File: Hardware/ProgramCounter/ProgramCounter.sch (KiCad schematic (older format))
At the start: 27 parts, among them J1 Conn_02x08, J2 Conn_02x08, J3 Conn_02x08, J4 Conn_02x08

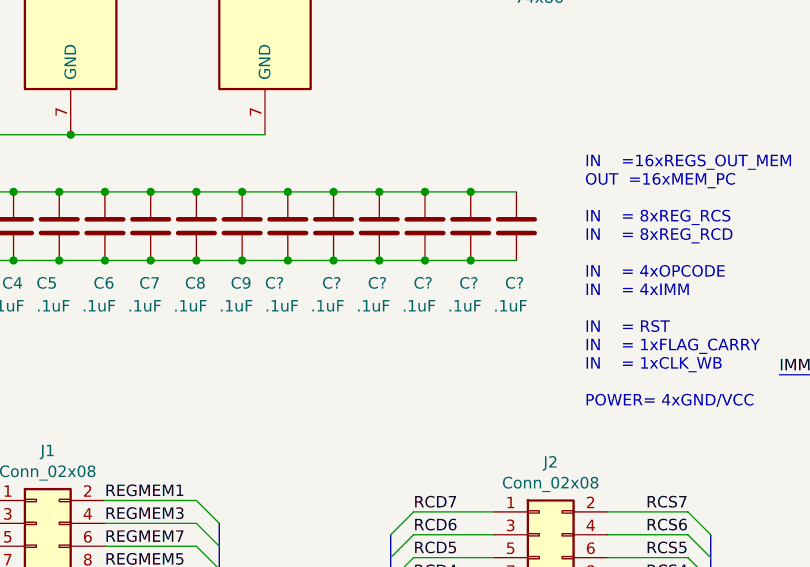
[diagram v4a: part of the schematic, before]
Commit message: PC Board
Mostly done. Going to move register to the right and connect logic gates
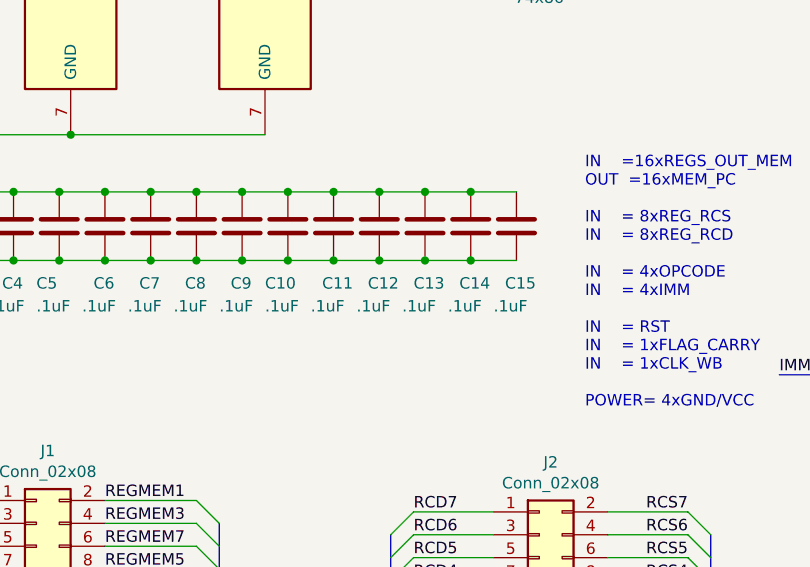
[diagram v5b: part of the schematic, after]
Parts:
- gave numbers to parts that had none: 6
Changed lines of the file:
@@
 $EndComp
 $Comp
-L Device:C C?
+L Device:C C10
 U 1 1 6294B873
 P 2600 5350
-F 0 "C?" H 2500 5100 50  0000 L CNN
+F 0 "C10" H 2500 5100 50  0000 L CNN
 F 1 ".1uF" H 2500 5000 50  0000 L CNN
 F 2 "Capacitor_SMD:C_1206_3216Metric_Pad1.42x1.75mm_HandSolder" H 2638 5200 50  0001 C CNN
@@
 $EndComp
 $Comp
-L Device:C C?
+L Device:C C11
 U 1 1 6294B879
 P 2800 5350
-F 0 "C?" H 2750 5100 50  0000 L CNN
+F 0 "C11" H 2750 5100 50  0000 L CNN
 F 1 ".1uF" H 2700 5000 50  0000 L CNN
 F 2 "Capacitor_SMD:C_1206_3216Metric_Pad1.42x1.75mm_HandSolder" H 2838 5200 50  0001 C CNN
@@
 $EndComp
 $Comp
-L Device:C C?
+L Device:C C12
 U 1 1 6294B87F
 P 3000 5350
-F 0 "C?" H 2950 5100 50  0000 L CNN
+F 0 "C12" H 2950 5100 50  0000 L CNN
 F 1 ".1uF" H 2900 5000 50  0000 L CNN
 F 2 "Capacitor_SMD:C_1206_3216Metric_Pad1.42x1.75mm_HandSolder" H 3038 5200 50  0001 C CNN
@@
 $EndComp
 $Comp
-L Device:C C?
+L Device:C C13
 U 1 1 6294B885
 P 3200 5350
-F 0 "C?" H 3150 5100 50  0000 L CNN
+F 0 "C13" H 3150 5100 50  0000 L CNN
 F 1 ".1uF" H 3100 5000 50  0000 L CNN
 F 2 "Capacitor_SMD:C_1206_3216Metric_Pad1.42x1.75mm_HandSolder" H 3238 5200 50  0001 C CNN
@@
 $EndComp
 $Comp
-L Device:C C?
+L Device:C C14
 U 1 1 6294B88B
 P 3400 5350
-F 0 "C?" H 3350 5100 50  0000 L CNN
+F 0 "C14" H 3350 5100 50  0000 L CNN
 F 1 ".1uF" H 3300 5000 50  0000 L CNN
 F 2 "Capacitor_SMD:C_1206_3216Metric_Pad1.42x1.75mm_HandSolder" H 3438 5200 50  0001 C CNN
@@
 $EndComp
 $Comp
-L Device:C C?
+L Device:C C15
 U 1 1 629609E2
 P 3600 5350
-F 0 "C?" H 3550 5100 50  0000 L CNN
+F 0 "C15" H 3550 5100 50  0000 L CNN
 F 1 ".1uF" H 3500 5000 50  0000 L CNN
 F 2 "Capacitor_SMD:C_1206_3216Metric_Pad1.42x1.75mm_HandSolder" H 3638 5200 50  0001 C CNN

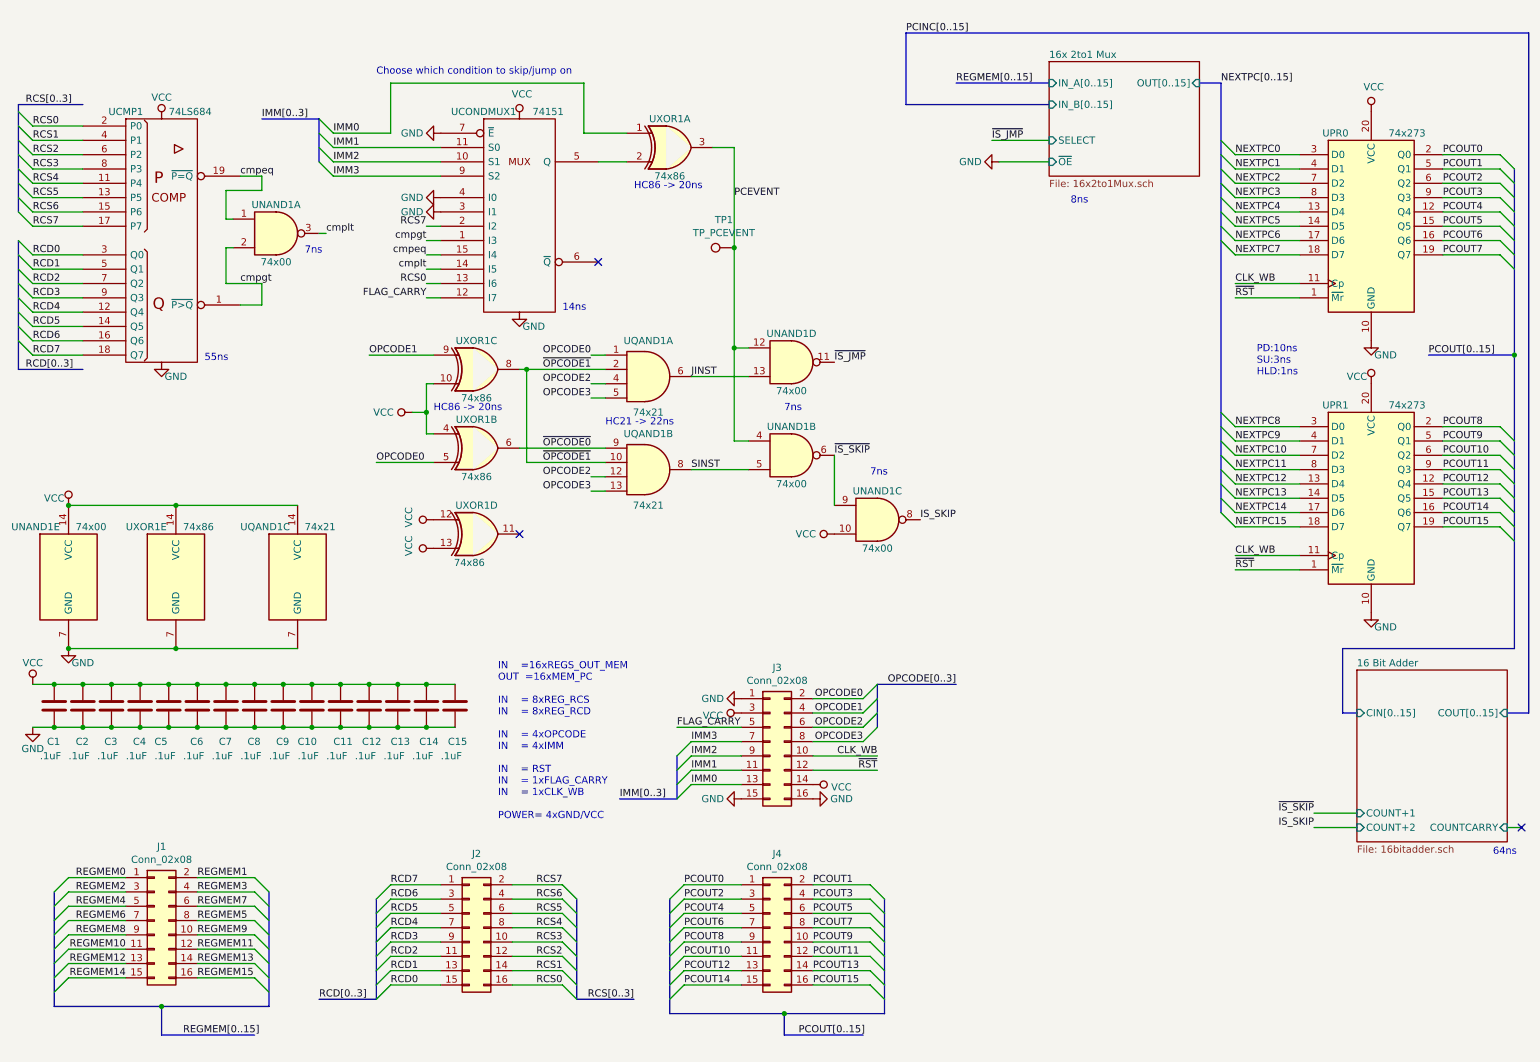
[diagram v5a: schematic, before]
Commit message: Program Counter Board
Seems to be done. Likely be ordering very soon. Also added a debug/testpoint connector to the top so that I can probe it easier
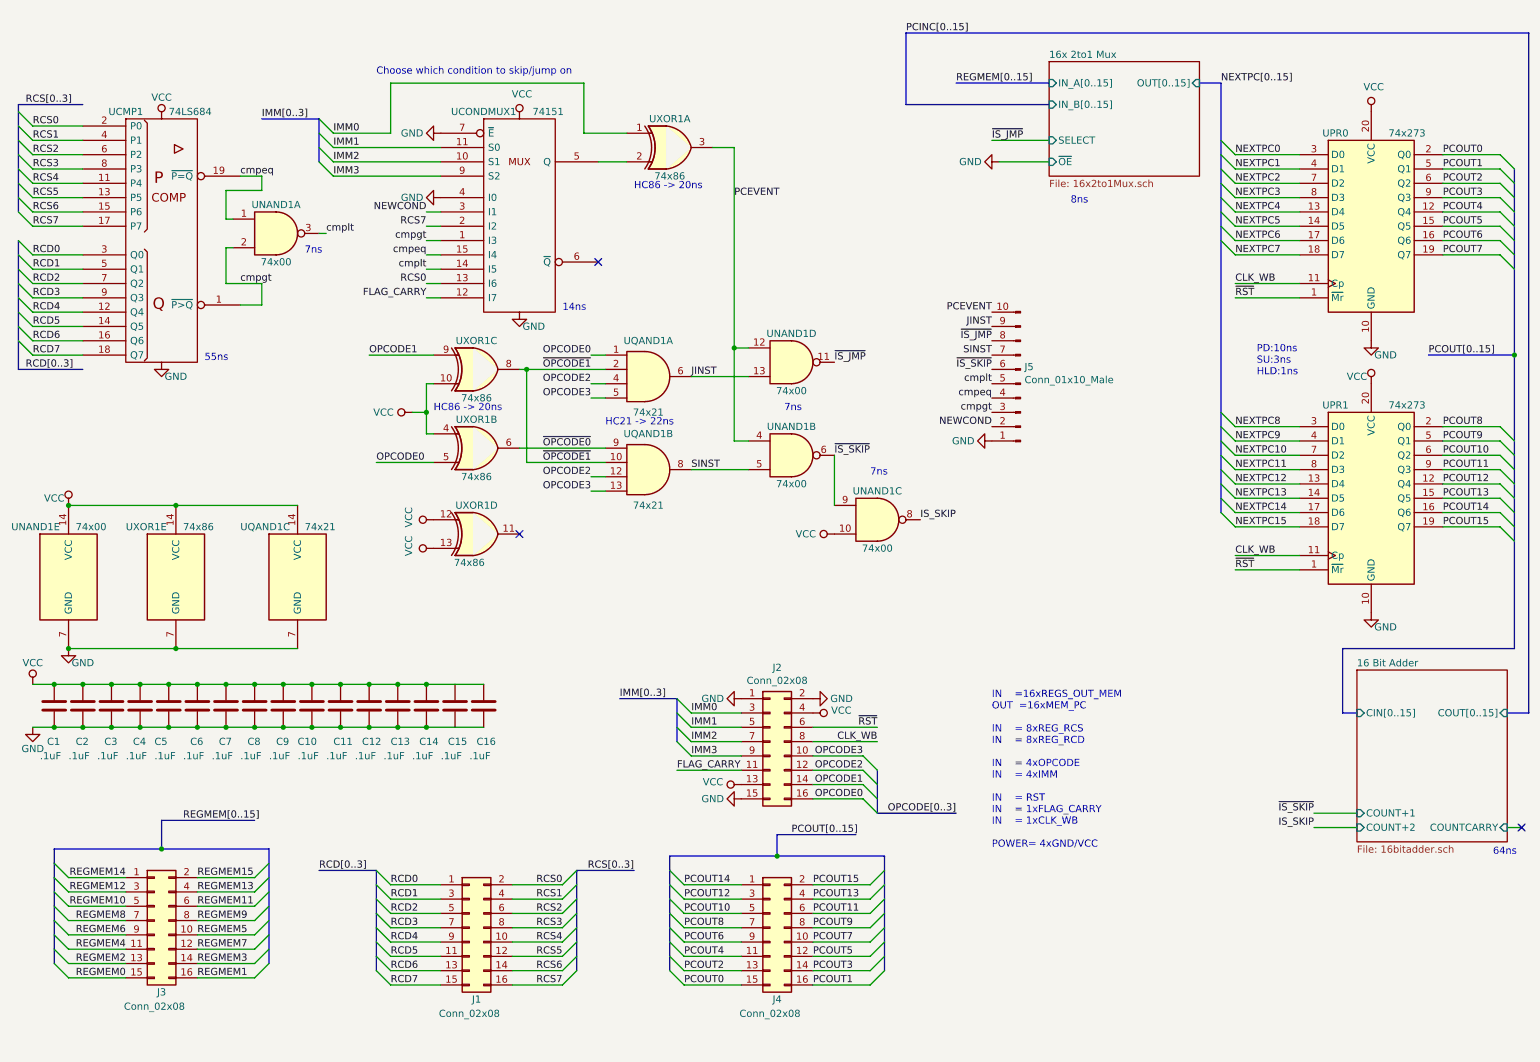
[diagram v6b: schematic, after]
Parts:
- removed TP1: TP_PCEVENT, Connector_PinHeader_2.54mm:PinHeader_1x01_P2.54mm_Vertical, symbol Connector:TestPoint
- added C16: .1uF, Capacitor_SMD:C_1206_3216Metric_Pad1.42x1.75mm_HandSolder, symbol Device:C
- added J5: Conn_01x10_Male, Connector_PinHeader_2.54mm:PinHeader_1x10_P2.54mm_Vertical, symbol Connector:Conn_01x10_Male
- J1: renamed from J2; footprint Connector_PinSocket_2.54mm:PinSocket_2x08_P2.54mm_Horizontal -> Connector_PinHeader_2.54mm:PinHeader_2x08_P2.54mm_Horizontal
- J2: renamed from J3; footprint Connector_PinSocket_2.54mm:PinSocket_2x08_P2.54mm_Horizontal -> Connector_PinHeader_2.54mm:PinHeader_2x08_P2.54mm_Horizontal
- J3: renamed from J1; footprint Connector_PinSocket_2.54mm:PinSocket_2x08_P2.54mm_Horizontal -> Connector_PinHeader_2.54mm:PinHeader_2x08_P2.54mm_Horizontal
- J4: footprint Connector_PinSocket_2.54mm:PinSocket_2x08_P2.54mm_Horizontal -> Connector_PinHeader_2.54mm:PinHeader_2x08_P2.54mm_Horizontal
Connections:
- net CLK_WB: now also J2.8 (Pin_8); no longer J2.10 (Pin_10)
- net FLAG_CARRY: now also J2.11 (Pin_11); no longer J2.5 (Pin_5)
- net GND: now also J2.2 (Pin_2), C16.2, J5.1 (Pin_1); no longer J2.16 (Pin_16), UCONDMUX1.3 (I1)
- net IMM0: now also J2.3 (Pin_3); no longer J2.13 (Pin_13)
- net IMM1: now also J2.5 (Pin_5); no longer J2.11 (Pin_11)
- net IMM2: now also J2.7 (Pin_7); no longer J2.9 (Pin_9)
- net IMM3: now also J2.9 (Pin_9); no longer J2.7 (Pin_7)
- net JINST: now also J5.9 (Pin_9)
- net OPCODE0: now also J2.16 (Pin_16); no longer J2.2 (Pin_2)
- net OPCODE1: now also J2.14 (Pin_14); no longer J2.4 (Pin_4)
- net OPCODE2: now also J2.12 (Pin_12); no longer J2.6 (Pin_6)
- net OPCODE3: now also J2.10 (Pin_10); no longer J2.8 (Pin_8)
- net PCEVENT: now also J5.10 (Pin_10)
- net PCOUT0: now also J4.15 (Pin_15); no longer J4.1 (Pin_1)
- net PCOUT1: now also J4.16 (Pin_16); no longer J4.2 (Pin_2)
- net PCOUT10: now also J4.5 (Pin_5); no longer J4.11 (Pin_11)
- net PCOUT11: now also J4.6 (Pin_6); no longer J4.12 (Pin_12)
- net PCOUT12: now also J4.3 (Pin_3); no longer J4.13 (Pin_13)
- net PCOUT13: now also J4.4 (Pin_4); no longer J4.14 (Pin_14)
- net PCOUT14: now also J4.1 (Pin_1); no longer J4.15 (Pin_15)
- net PCOUT15: now also J4.2 (Pin_2); no longer J4.16 (Pin_16)
- net PCOUT2: now also J4.13 (Pin_13); no longer J4.3 (Pin_3)
- net PCOUT3: now also J4.14 (Pin_14); no longer J4.4 (Pin_4)
- net PCOUT4: now also J4.11 (Pin_11); no longer J4.5 (Pin_5)
- net PCOUT5: now also J4.12 (Pin_12); no longer J4.6 (Pin_6)
- net PCOUT6: now also J4.9 (Pin_9); no longer J4.7 (Pin_7)
- net PCOUT7: now also J4.10 (Pin_10); no longer J4.8 (Pin_8)
- net PCOUT8: now also J4.7 (Pin_7); no longer J4.9 (Pin_9)
- net PCOUT9: now also J4.8 (Pin_8); no longer J4.10 (Pin_10)
- net RCD0: now also J1.1 (Pin_1); no longer J1.15 (Pin_15)
- net RCD1: now also J1.3 (Pin_3); no longer J1.13 (Pin_13)
- net RCD2: now also J1.5 (Pin_5); no longer J1.11 (Pin_11)
- net RCD3: now also J1.7 (Pin_7); no longer J1.9 (Pin_9)
- net RCD4: now also J1.9 (Pin_9); no longer J1.7 (Pin_7)
- net RCD5: now also J1.11 (Pin_11); no longer J1.5 (Pin_5)
- net RCD6: now also J1.13 (Pin_13); no longer J1.3 (Pin_3)
- net RCD7: now also J1.15 (Pin_15); no longer J1.1 (Pin_1)
- net RCS0: now also J1.2 (Pin_2); no longer J1.16 (Pin_16)
- net RCS1: now also J1.4 (Pin_4); no longer J1.14 (Pin_14)
- net RCS2: now also J1.6 (Pin_6); no longer J1.12 (Pin_12)
- net RCS3: now also J1.8 (Pin_8); no longer J1.10 (Pin_10)
- net RCS4: now also J1.10 (Pin_10); no longer J1.8 (Pin_8)
- net RCS5: now also J1.12 (Pin_12); no longer J1.6 (Pin_6)
- net RCS6: now also J1.14 (Pin_14); no longer J1.4 (Pin_4)
- net RCS7: now also J1.16 (Pin_16); no longer J1.2 (Pin_2)
- net REGMEM0: now also J3.15 (Pin_15); no longer J3.1 (Pin_1)
- net REGMEM1: now also J3.16 (Pin_16); no longer J3.2 (Pin_2)
- net REGMEM10: now also J3.5 (Pin_5); no longer J3.11 (Pin_11)
- net REGMEM11: now also J3.6 (Pin_6); no longer J3.12 (Pin_12)
- net REGMEM12: now also J3.3 (Pin_3); no longer J3.13 (Pin_13)
- net REGMEM13: now also J3.4 (Pin_4); no longer J3.14 (Pin_14)
- net REGMEM14: now also J3.1 (Pin_1); no longer J3.15 (Pin_15)
- net REGMEM15: now also J3.2 (Pin_2); no longer J3.16 (Pin_16)
- net REGMEM2: now also J3.13 (Pin_13); no longer J3.3 (Pin_3)
- net REGMEM3: now also J3.14 (Pin_14); no longer J3.4 (Pin_4)
- net REGMEM4: now also J3.11 (Pin_11); no longer J3.5 (Pin_5)
- net REGMEM5: now also J3.10 (Pin_10); no longer J3.8 (Pin_8)
- net REGMEM6: now also J3.9 (Pin_9); no longer J3.7 (Pin_7)
- net REGMEM7: now also J3.12 (Pin_12); no longer J3.6 (Pin_6)
- net REGMEM8: now also J3.7 (Pin_7); no longer J3.9 (Pin_9)
- net REGMEM9: now also J3.8 (Pin_8); no longer J3.10 (Pin_10)
- net SINST: now also J5.7 (Pin_7)
- net VCC: now also J2.13 (Pin_13), J2.4 (Pin_4), C16.1; no longer J2.14 (Pin_14), J2.3 (Pin_3)
- net cmpeq: now also J5.4 (Pin_4)
- net cmpgt: now also J5.3 (Pin_3)
- net cmplt: now also J5.5 (Pin_5)
- net ~IS_JMP: now also J5.8 (Pin_8)
- net ~IS_SKIP: now also J5.6 (Pin_6)
- net ~RST: now also J2.6 (Pin_6); no longer J2.12 (Pin_12)
- new net NEWCOND: J5.2 (Pin_2), UCONDMUX1.3 (I1)

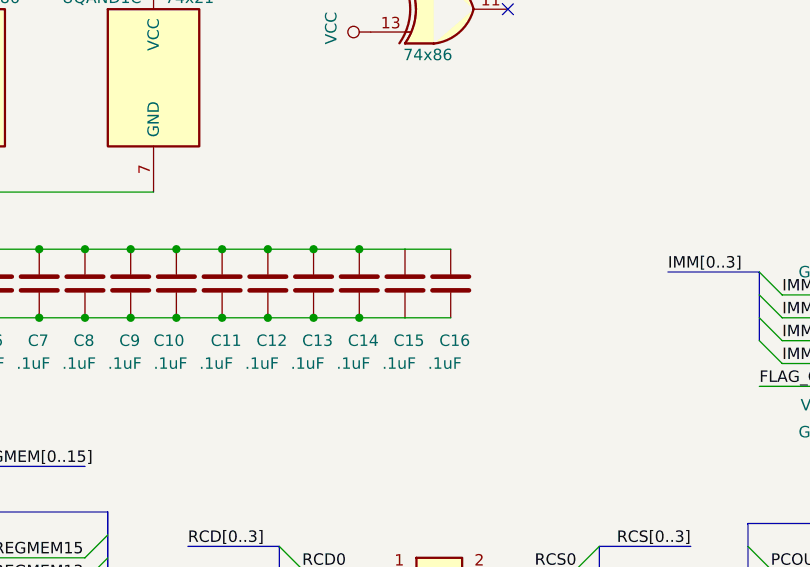
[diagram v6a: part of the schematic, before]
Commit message: Created export for Program Counter PCB V1
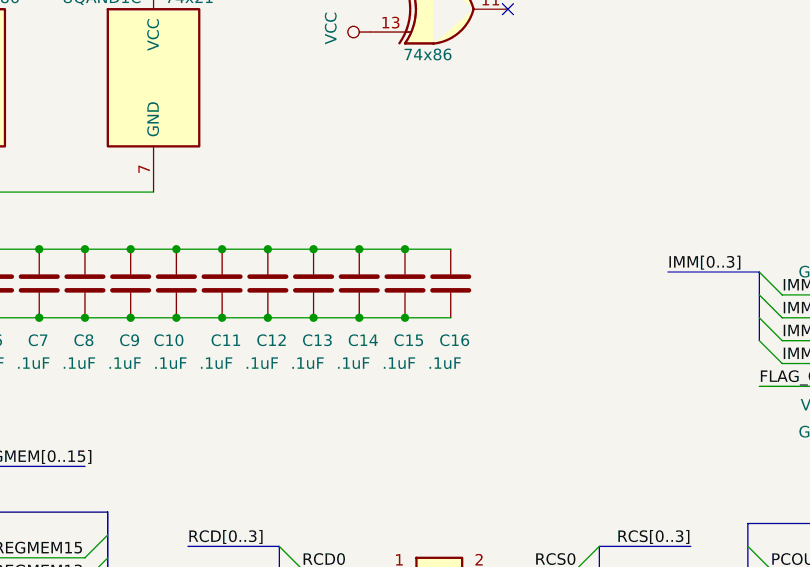
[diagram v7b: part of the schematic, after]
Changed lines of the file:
@@
 Wire Bus Line
 	8950 1000 8950 4000
+Connection ~ 3600 5200
+Connection ~ 3600 5500
 $EndSCHEMATC
